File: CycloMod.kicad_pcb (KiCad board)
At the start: 4 copper layers, 22 x 22 mm, 66 parts, among them J1 MICROMOD-2222, U1 10CL010YM164, U2 W25Q128JVS, U3 1.2V, U4 RP2350_60QFN, U5 MIC5504-2.5YMT, Y1 ABM8-272-T3

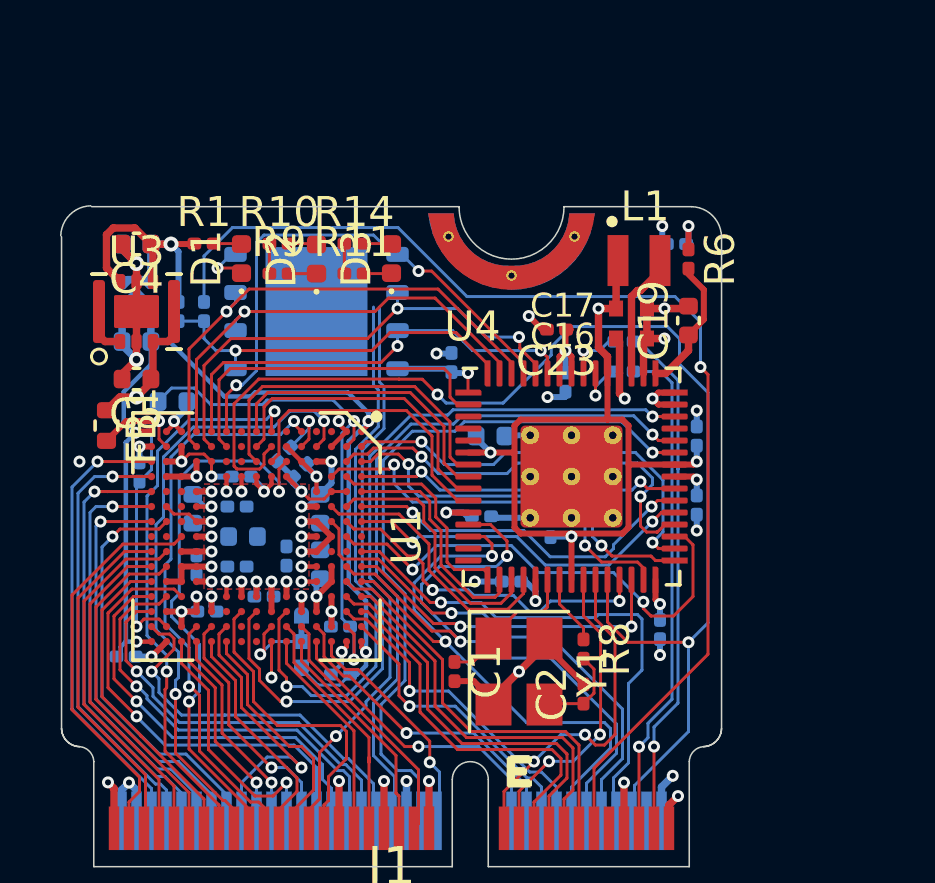
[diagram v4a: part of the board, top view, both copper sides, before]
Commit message: checking in fully placed and routed.  still needs silkscreen and cleanup
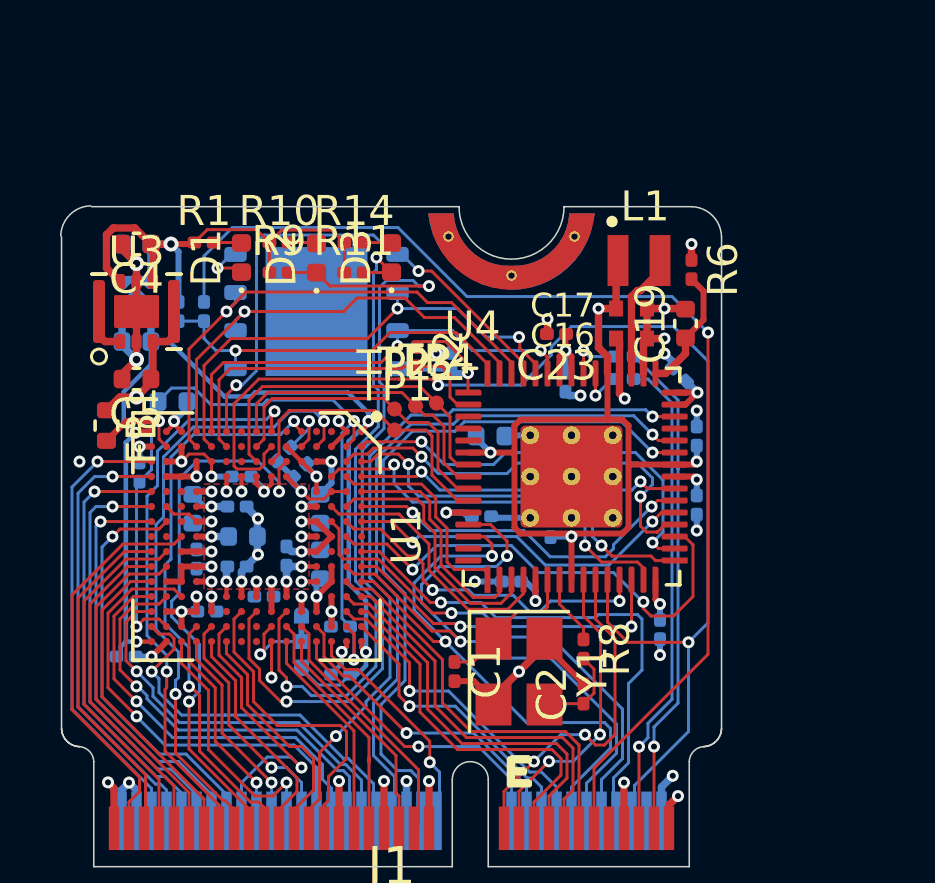
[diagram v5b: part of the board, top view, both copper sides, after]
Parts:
- added R2: 10k, Resistor_SMD:R_0201_0603Metric, F.Cu at (149.3, 99.0)
- added TP1: TDI, custom:TestPoint_Pad_D0.5mm, F.Cu at (148.6, 101.5)
- added TP2: TCK, custom:TestPoint_Pad_D0.5mm, F.Cu at (148.6, 100.8)
- added TP3: TMS, custom:TestPoint_Pad_D0.5mm, F.Cu at (149.3, 100.7)
- added TP4: TDO, custom:TestPoint_Pad_D0.5mm, F.Cu at (150.0, 100.5)
- moved C27 4.35 mm to (158.1, 99.6), turned to 135 degrees
- moved R12 0.50 mm to (156.2, 99.0)
- moved R6 0.36 mm to (158.5, 96.1)
- moved R13 0.25 mm to (156.2, 99.8)
- moved C12 0.20 mm to (142.0, 105.8)
- moved C23 0.15 mm to (154.0, 98.2)
- moved C19 0.14 mm to (158.3, 97.9)
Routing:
- net +3V3: track 45.3 -> 54.1 mm
- net /DONE: track 21.0 -> 27.4 mm, vias 1 -> 2
- net GND: track 67.5 -> 72.3 mm, vias 43 -> 45
- net /INIT: track 19.8 -> 22.2 mm, vias 1 -> 2
- net +1V2: track 22.4 -> 24.5 mm

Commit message: started silkscreen cleanup, checking in prior to cardedge/outline update
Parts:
- added R4: 10k, Resistor_SMD:R_0201_0603Metric, F.Cu at (156.5, 109.0)
- FB1: value FerriteBead_Small -> 120
- LOGO3: moved to B.Cu
- moved LOGO3 72.1 mm to (151.1, 111.2), turned to 180 degrees
- moved C38 12.1 mm to (157.0, 110.5)
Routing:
- net /CLKIN1: track 14.2 -> 13.3 mm
- net /~{BOOT}: track 38.3 -> 39.2 mm
- net +3V3: track 54.1 -> 54.6 mm, vias 19 -> 20
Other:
- board text added: "!DONE"
- board text added: "JT AS"
- board text added: "POWER"
- board text added: "USER"

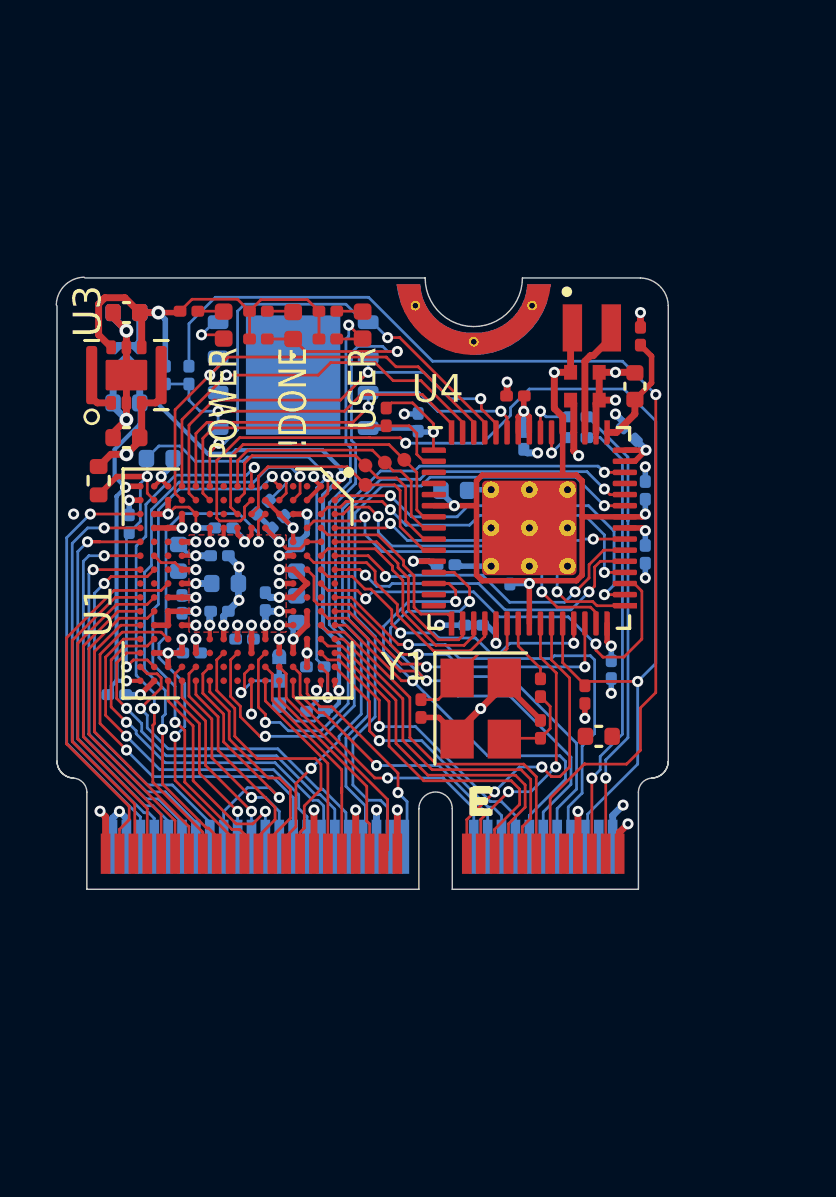
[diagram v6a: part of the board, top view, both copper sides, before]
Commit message: updated micromod footprint, more KiCad native
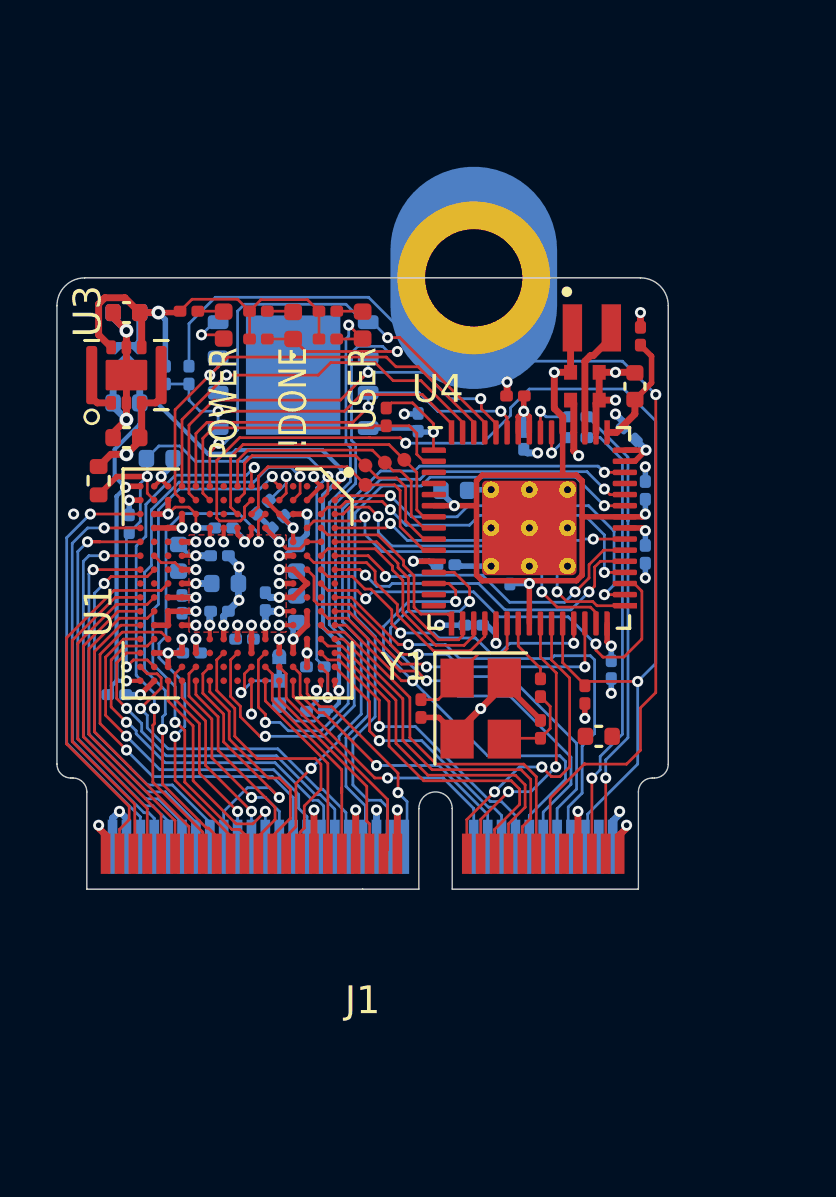
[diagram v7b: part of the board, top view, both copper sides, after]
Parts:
- J1: footprint MicroMod-RP2040-ProcessorBoard:M.2-CARD-E-22 -> custom:MicroMod_Processor
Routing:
- net GND: track 72.3 -> 71.8 mm
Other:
- outline, holes or cut-outs redrawn

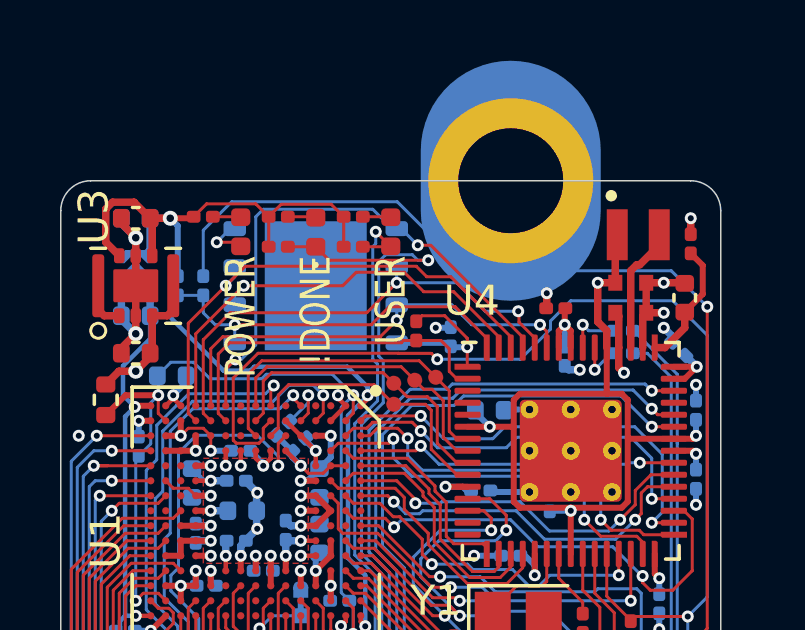
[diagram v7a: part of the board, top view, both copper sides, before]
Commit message: remaped QSPI pins, checking in before moving flash
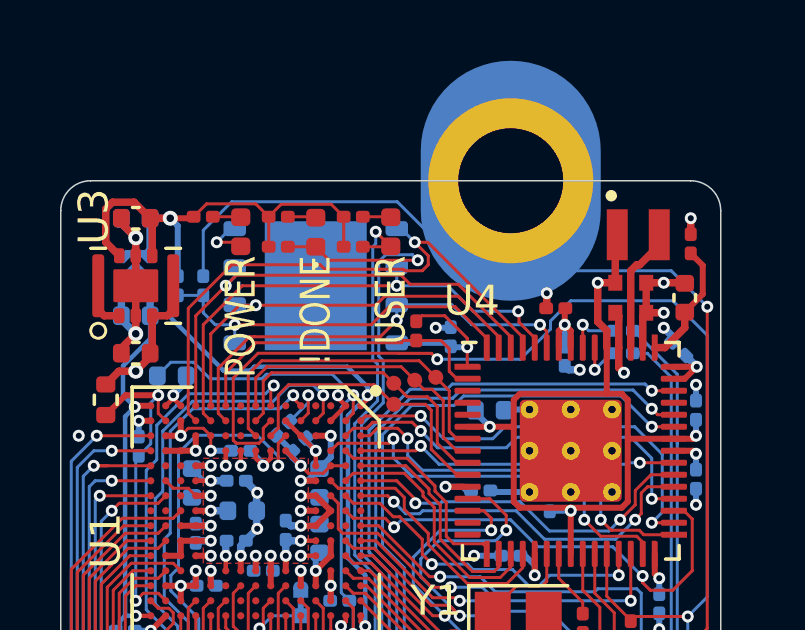
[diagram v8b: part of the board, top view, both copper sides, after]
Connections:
- U1 pad K1: /QSPI_SD0 -> /QSPI_SS1
- U1 pad K2: /QSPI_SS1 -> /QSPI_SD3
- U1 pad L1: /QSPI_SD3 -> /QSPI_SD1
- U1 pad M1: /QSPI_SD1 -> /QSPI_SD2
- U1 pad M2: /QSPI_SD2 -> /QSPI_SD0
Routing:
- net /QSPI_SD0: track 18.0 -> 19.6 mm, vias 2 -> 1
- net /QSPI_SS1: track 11.8 -> 10.6 mm
- net /QSPI_SD1: track 15.4 -> 14.1 mm
- net /QSPI_SD2: track 17.0 -> 16.0 mm
- net /DONE: track 27.4 -> 26.7 mm
